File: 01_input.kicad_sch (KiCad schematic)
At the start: 27 parts, among them J1 0533980471, U1 VOS618A, U2 LMR51406YDBV

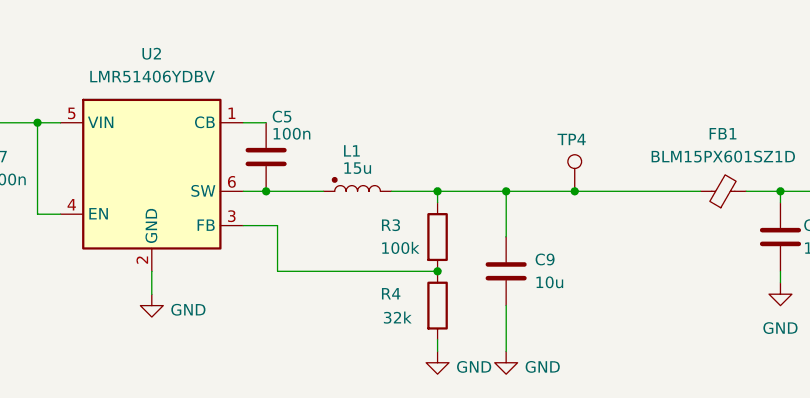
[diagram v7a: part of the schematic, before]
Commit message: Add MPN and DigiKey PN to all components
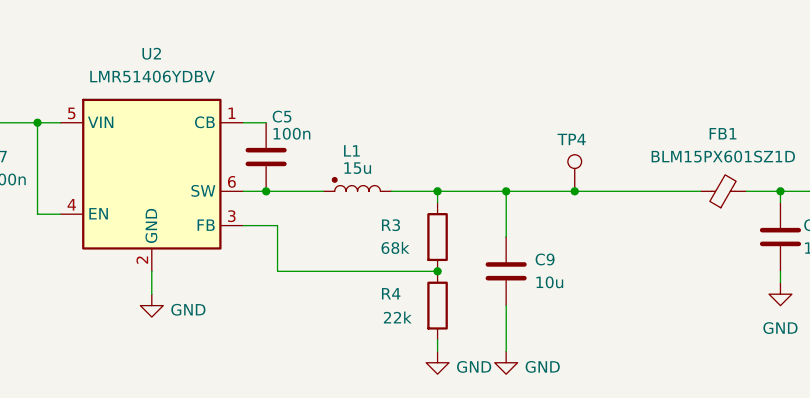
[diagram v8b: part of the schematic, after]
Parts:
- C1, C2: DigiKey PN (none) -> 1276-6733-1-ND
- C3, C4: DigiKey PN (none) -> 587-HMK105B7103KVHFECT-ND; MPN (none) -> HMK105B7103KVHFE
- C5, C7, C8: DigiKey PN (none) -> 1276-6720-1-ND; MPN (none) -> CL05B104KA5NNNC
- C6: DigiKey PN (none) -> 1276-CL31B475KBHVPJECT-ND
- C9: DigiKey PN (none) -> 1276-1804-1-ND
- D1: DigiKey PN (none) -> 1727-5846-1-ND; MPN (none) -> PMEG6010ER,115
- D2: DigiKey PN (none) -> SMAJ30CALFCT-ND; MPN (none) -> SMAJ30CA
- D3: DigiKey PN (none) -> VESD05B1-02V-G3-08GICT-ND; MPN (none) -> VESD05B1-02V-G3-08
- F1: DigiKey PN (none) -> 478-F0603G0R15FNCT-ND; MPN (none) -> F0603G0R15FNTR; Mouser No (none) -> 581-F0603G0R15FNTR
- FB1: DigiKey PN (none) -> 490-16655-1-ND; MPN (none) -> BLM15PX601SZ1D
- J1: DigiKey PN (none) -> WM7608CT-ND; MPN (none) -> 0533980471
- L1: DigiKey PN (none) -> 445-VLS3015CX-150M-HCT-ND
- R1: DigiKey PN (none) -> 311-5.6KLRCT-ND; MPN (none) -> RC0402FR-075K6L
- R2: DigiKey PN (none) -> 311-1.80KLRCT-ND; MPN (none) -> RC0402FR-071K8L
- R3: value 100k -> 68k; DigiKey PN (none) -> 311-68.0KLRCT-ND; MPN (none) -> RC0402FR-0768KL
- R4: value 32k -> 22k; DigiKey PN (none) -> 311-22.0KLRCT-ND; MPN (none) -> RC0402FR-0722KL
- U1: DigiKey PN (none) -> VOS618A-3X001TCT-ND; MPN (none) -> VOS618A-3X001T
- U2: DigiKey PN (none) -> 296-LMR51406YDBVRCT-ND; MPN (none) -> LMR51406YDBV
